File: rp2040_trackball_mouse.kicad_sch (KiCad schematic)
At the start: 29 parts, among them J1 Conn_01x05, J2 Conn_01x06, J5 Conn_02x08_Odd_Even, J6 Conn_02x08_Odd_Even, SW1 SW_Push, SW2 SW_Push, SW3 SW_Push, SW4 SW_Push, U1 NJM4580, U2 PT5529B/L2/H3

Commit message: 回路図を更新
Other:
- moved on the sheet: R12, R14, R17, R18, R22, R23, R26, U1A, U1B

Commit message: ホイールがぎこちないのを記述
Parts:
- U1: value NJM4580 -> LMV393D
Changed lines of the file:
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@@
     (in_bom yes) (on_board yes)
     (property "Reference" "U1" (id 0) (at 248.92 26.2382 0))
-    (property "Value" "NJM4580" (id 1) (at 248.92 28.5496 0))
+    (property "Value" "LMV393D" (id 1) (at 248.92 28.5496 0))
     (property "Footprint" "Package_SO:SOP-8_3.9x4.9mm_P1.27mm" (id 2) (at 248.92 35.56 0)
       (effects (font (size 1.27 1.27)) hide)
     )
-    (property "Datasheet" "https://akizukidenshi.com/catalog/g/gI-14003/" (id 3) (at 248.92 35.56 0)
+    (property "Datasheet" "https://www.marutsu.co.jp/pc/i/30637519/" (id 3) (at 248.92 35.56 0)
       (effects (font (size 1.27 1.27)) hide)
     )
@@
     (in_bom yes) (on_board yes)
     (property "Reference" "U1" (id 0) (at 248.285 77.0382 0))
-    (property "Value" "NJM4580" (id 1) (at 248.285 79.3496 0))
+    (property "Value" "LMV393D" (id 1) (at 248.285 79.3496 0))
     (property "Footprint" "Package_SO:SOP-8_3.9x4.9mm_P1.27mm" (id 2) (at 248.285 86.36 0)
       (effects (font (size 1.27 1.27)) hide)
     )
-    (property "Datasheet" "https://akizukidenshi.com/catalog/g/gI-14003/" (id 3) (at 248.285 86.36 0)
+    (property "Datasheet" "https://www.marutsu.co.jp/pc/i/30637519/" (id 3) (at 248.285 86.36 0)
       (effects (font (size 1.27 1.27)) hide)
     )
@@
       (effects (font (size 1.27 1.27)) (justify left))
     )
-    (property "Value" "NJM4580" (id 1) (at 165.9382 178.943 0)
+    (property "Value" "LMV393D" (id 1) (at 165.9382 178.943 0)
       (effects (font (size 1.27 1.27)) (justify left))
     )
@@
       (effects (font (size 1.27 1.27)) hide)
     )
-    (property "Datasheet" "https://akizukidenshi.com/catalog/g/gI-14003/" (id 3) (at 167.005 177.8 0)
+    (property "Datasheet" "https://www.marutsu.co.jp/pc/i/30637519/" (id 3) (at 167.005 177.8 0)
       (effects (font (size 1.27 1.27)) hide)
     )
@@
     )
     (path "/00000000-0000-0000-0000-0000615ef3ec"
-      (reference "U1") (unit 1) (value "NJM4580") (footprint "Package_SO:SOP-8_3.9x4.9mm_P1.27mm")
+      (reference "U1") (unit 1) (value "LMV393D") (footprint "Package_SO:SOP-8_3.9x4.9mm_P1.27mm")
     )
     (path "/00000000-0000-0000-0000-0000615f1cc6"
-      (reference "U1") (unit 2) (value "NJM4580") (footprint "Package_SO:SOP-8_3.9x4.9mm_P1.27mm")
+      (reference "U1") (unit 2) (value "LMV393D") (footprint "Package_SO:SOP-8_3.9x4.9mm_P1.27mm")
     )
     (path "/00000000-0000-0000-0000-0000615f261a"
-      (reference "U1") (unit 3) (value "NJM4580") (footprint "Package_SO:SOP-8_3.9x4.9mm_P1.27mm")
+      (reference "U1") (unit 3) (value "LMV393D") (footprint "Package_SO:SOP-8_3.9x4.9mm_P1.27mm")
     )
     (path "/00000000-0000-0000-0000-0000614734e8"

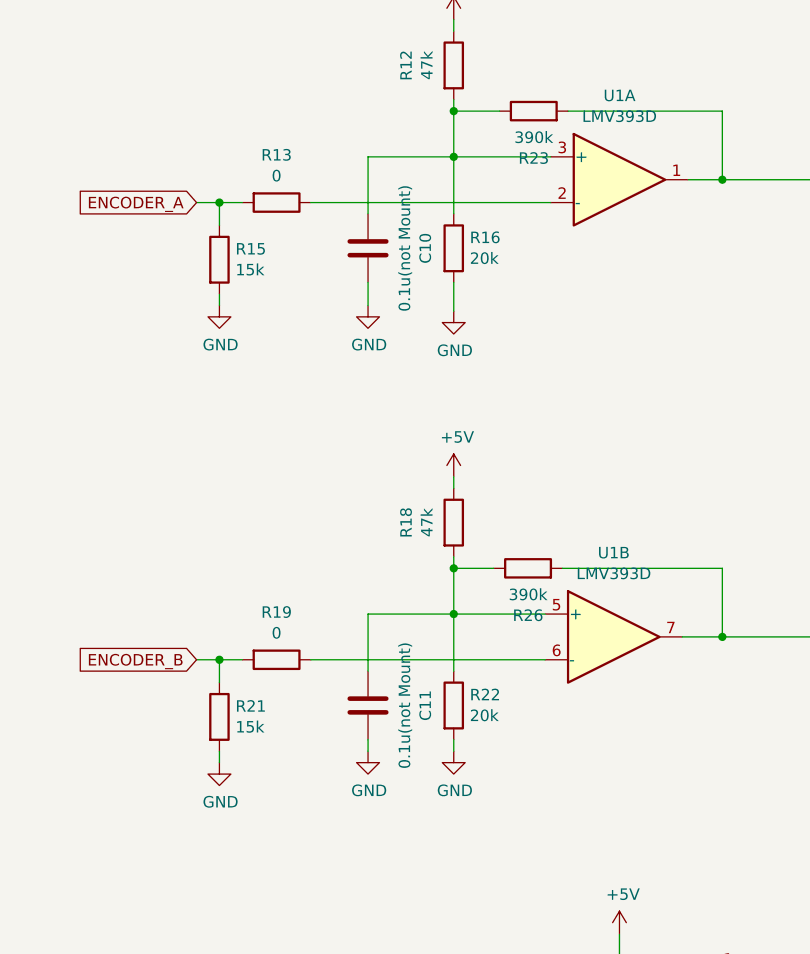
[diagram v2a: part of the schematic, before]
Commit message: 仮に入れていた値を削除
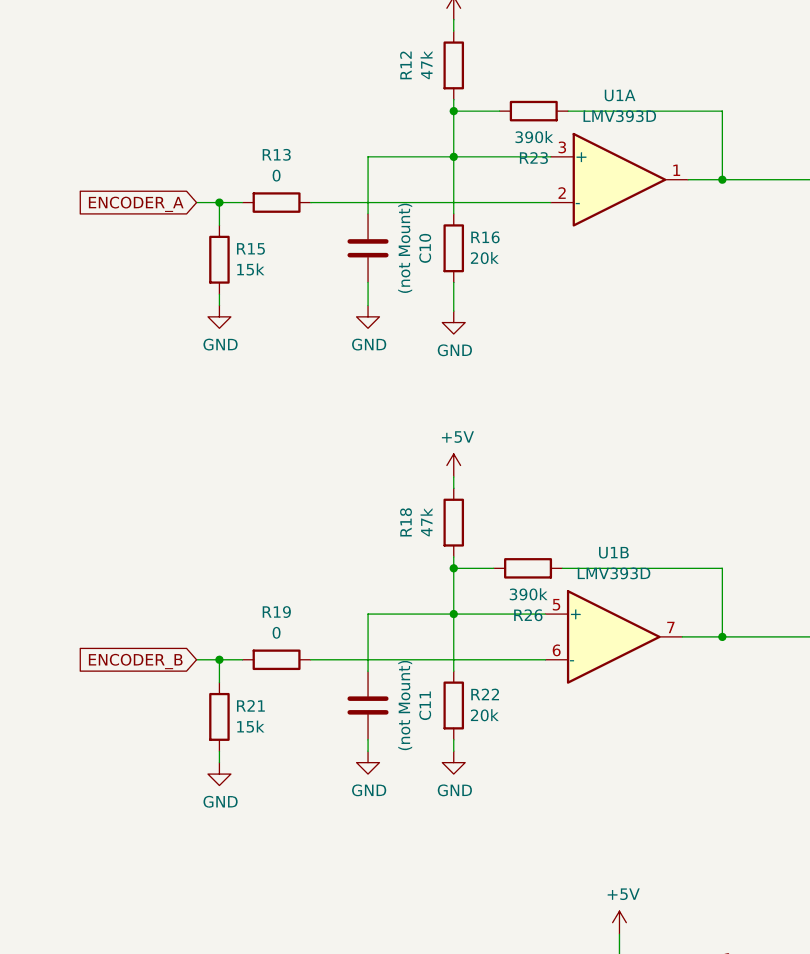
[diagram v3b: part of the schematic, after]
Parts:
- C10, C11: value 0.1u(not Mount) -> (not Mount)
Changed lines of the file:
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@@
     (in_bom yes) (on_board yes)
     (property "Reference" "C10" (id 0) (at 227.3808 43.18 90))
-    (property "Value" "0.1u(not Mount)" (id 1) (at 225.0694 43.18 90))
+    (property "Value" "(not Mount)" (id 1) (at 225.0694 43.18 90))
     (property "Footprint" "Capacitor_SMD:C_0603_1608Metric_Pad1.08x0.95mm_HandSolder" (id 2) (at 220.0148 39.37 0)
       (effects (font (size 1.27 1.27)) hide)
@@
     (in_bom yes) (on_board yes)
     (property "Reference" "C11" (id 0) (at 227.3808 93.98 90))
-    (property "Value" "0.1u(not Mount)" (id 1) (at 225.0694 93.98 90))
+    (property "Value" "(not Mount)" (id 1) (at 225.0694 93.98 90))
     (property "Footprint" "Capacitor_SMD:C_0603_1608Metric_Pad1.08x0.95mm_HandSolder" (id 2) (at 221.9452 97.79 0)
       (effects (font (size 1.27 1.27)) hide)
@@
     )
     (path "/00000000-0000-0000-0000-00006145a14b"
-      (reference "C10") (unit 1) (value "0.1u(not Mount)") (footprint "Capacitor_SMD:C_0603_1608Metric_Pad1.08x0.95mm_HandSolder")
+      (reference "C10") (unit 1) (value "(not Mount)") (footprint "Capacitor_SMD:C_0603_1608Metric_Pad1.08x0.95mm_HandSolder")
     )
     (path "/00000000-0000-0000-0000-00006145aa75"
-      (reference "C11") (unit 1) (value "0.1u(not Mount)") (footprint "Capacitor_SMD:C_0603_1608Metric_Pad1.08x0.95mm_HandSolder")
+      (reference "C11") (unit 1) (value "(not Mount)") (footprint "Capacitor_SMD:C_0603_1608Metric_Pad1.08x0.95mm_HandSolder")
     )
     (path "/00000000-0000-0000-0000-000061436811"
